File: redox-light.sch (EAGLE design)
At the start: 128 parts, among them IC36 STM32F103TXUX, X2 USBMICRO_B, X3 AUDIO-JACKSMD

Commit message: layout template
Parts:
- added IC38: 74HC595BQ, netcat:74HC595BQ
- added IC39: W25Q64FV, netcat:W25Q64FV
- C2: device netcat:CAP0402 -> netcat:CPOL-EUSMCA
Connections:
- removed net N$35: C1.+, IC37.IN, X2.VBUS
- new net FLASH_CS: IC36GPIOA.PA15, IC39.!CS
- new net SPI_MISO: IC36GPIOB.PB4, IC39.MISO/IO1
- new net SPI_MOSI: IC36GPIOB.PB5, IC39.MOSI/IO0
- new net SPI_SCL: IC36GPIOB.PB3, IC39.SCK
- new net SR_CLK: IC36GPIOB.PB1, IC38.SHCP, IC38.STCP
- new net SR_CLR: IC36GPIOB.PB2, IC38.!MR
- new net SR_D: IC36GPIOB.PB0, IC38.DS
- net !BL_EN: now also IC36GPIOA.PA8; no longer IC36GPIOB.PB5
- net 5V: now also C1.+, IC37.IN, X2.VBUS
- net BL_SDI: now also IC36GPIOA.PA7; no longer IC36GPIOA.PA8
- net GND: now also C2.-, IC38.!OE, IC38.GND, IC39.GND; no longer C2.2
- net N$17: now also VD4.C; no longer VD4.A
- net N$18: now also VD3.C; no longer VD3.A
- net N$19: now also VD5.C; no longer VD5.A
- net N$20: now also VD6.C; no longer VD6.A
- net N$21: now also VD2.C; no longer VD2.A
- net N$22: now also VD13.C; no longer VD13.A
- net N$24: now also VD7.C; no longer VD7.A
- net N$25: now also VD8.C; no longer VD8.A
- net N$26: now also VD9.C; no longer VD9.A
- net N$27: now also VD10.C; no longer VD10.A
- net N$28: now also VD11.C; no longer VD11.A
- net N$29: now also VD12.C; no longer VD12.A
- net N$30: now also VD20.C; no longer VD20.A
- net N$46: now also VD14.C; no longer VD14.A
- net N$47: now also VD15.C; no longer VD15.A
- net N$48: now also VD16.C; no longer VD16.A
- net N$49: now also VD17.C; no longer VD17.A
- net N$50: now also VD18.C; no longer VD18.A
- net N$51: now also VD19.C; no longer VD19.A
- net N$54: now also VD21.C; no longer VD21.A
- net N$55: now also VD22.C; no longer VD22.A
- net N$56: now also VD29.C; no longer VD29.A
- net N$57: now also VD30.C; no longer VD30.A
- net N$58: now also VD23.C; no longer VD23.A
- net N$59: now also VD24.C; no longer VD24.A
- net N$60: now also VD25.C; no longer VD25.A
- net N$61: now also VD26.C; no longer VD26.A
- net N$62: now also VD27.C; no longer VD27.A
- net N$63: now also VD28.C; no longer VD28.A
- net N$64: now also VD31.C; no longer VD31.A
- net N$65: now also VD32.C; no longer VD32.A
- net N$66: now also VD33.C; no longer VD33.A
- net N$67: now also VD34.C; no longer VD34.A
- net N$68: now also VD35.C; no longer VD35.A
- net N$7: now also VD1.C; no longer VD1.A
- net ROW0: now also IC38.Q0, VD1.A, VD13.A, VD2.A, VD3.A, VD4.A, VD5.A, VD6.A; no longer IC36GPIOB.PB0, VD1.C, VD13.C, VD2.C, VD3.C, VD4.C, VD5.C, VD6.C
- net ROW1: now also IC38.Q1, VD10.A, VD11.A, VD12.A, VD20.A, VD7.A, VD8.A, VD9.A; no longer IC36GPIOB.PB1, VD10.C, VD11.C, VD12.C, VD20.C, VD7.C, VD8.C, VD9.C
- net ROW2: now also IC38.Q2, VD14.A, VD15.A, VD16.A, VD17.A, VD18.A, VD19.A, VD27.A; no longer IC36GPIOB.PB2, VD14.C, VD15.C, VD16.C, VD17.C, VD18.C, VD19.C, VD27.C
- net ROW3: now also IC38.Q3, VD21.A, VD22.A, VD23.A, VD24.A, VD25.A, VD26.A, VD28.A; no longer IC36GPIOB.PB3, VD21.C, VD22.C, VD23.C, VD24.C, VD25.C, VD26.C, VD28.C
- net ROW4: now also IC38.Q4, VD29.A, VD30.A, VD31.A, VD32.A, VD33.A, VD34.A, VD35.A; no longer IC36GPIOB.PB4, VD29.C, VD30.C, VD31.C, VD32.C, VD33.C, VD34.C, VD35.C
- net VCC: now also C2.+, IC38.VCC, IC39.VCC; no longer C2.1
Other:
- moved on the sheet: VD1, VD10, VD11, VD12, VD13, VD14, VD15, VD16, VD17, VD18, VD19, VD2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

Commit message: aligned buttons, board layout completed
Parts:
- removed Q2: (no value), netcat:MOSFET_PSOT23
- removed R8: 100k, netcat:RESR0402
- removed X3: AUDIO-JACKSMD, netcat:AUDIO-JACKSMD
- removed X4: (no value), netcat:M03
- added C15, C16, C17, C18, C20, C21: (no value), netcat:CAP0402
- added C19: (no value), netcat:CPOL-EUSMCA
- added R2, R3: 4.7k, netcat:RESR0402
- added X1: USBMICRO_B, netcat:USBMICRO_B
- X2: value USBMICRO_B -> AUDIO-JACKSMD; device netcat:USBMICRO_B -> netcat:AUDIO-JACKSMD
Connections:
- removed net !BL_EN: IC36GPIOA.PA8, Q2.G, R8.2
- removed net VCC_LEDS: C10.1, C11.1, C12.1, C3.1, C4.1, C5.1, C6.1, C7.1, C8.1, C9.1, IC1.VCC, IC10.VCC, IC11.VCC, IC12.VCC, IC13.VCC, IC14.VCC, IC15.VCC, IC16.VCC, IC17.VCC, IC18.VCC, IC19.VCC, IC2.VCC, IC20.VCC, IC21.VCC, IC22.VCC, IC23.VCC, IC24.VCC, IC25.VCC, IC26.VCC, IC27.VCC, IC28.VCC, IC29.VCC, IC3.VCC, IC30.VCC, IC31.VCC, IC32.VCC, IC33.VCC, IC34.VCC, IC35.VCC, IC4.VCC, IC5.VCC, IC6.VCC, IC7.VCC, IC8.VCC, IC9.VCC, Q2.D
- net 5V: now also C10.1, C11.1, C12.1, C13.1, C14.1, C15.1, C16.1, C17.1, C18.1, C3.1, C4.1, C5.1, C6.1, C7.1, C8.1, C9.1, IC1.VCC, IC10.VCC, IC11.VCC, IC12.VCC, IC13.VCC, IC14.VCC, IC15.VCC, IC16.VCC, IC17.VCC, IC18.VCC, IC19.VCC, IC2.VCC, IC20.VCC, IC21.VCC, IC22.VCC, IC23.VCC, IC24.VCC, IC25.VCC, IC26.VCC, IC27.VCC, IC28.VCC, IC29.VCC, IC3.VCC, IC30.VCC, IC31.VCC, IC32.VCC, IC33.VCC, IC34.VCC, IC35.VCC, IC4.VCC, IC5.VCC, IC6.VCC, IC7.VCC, IC8.VCC, IC9.VCC, X1.VBUS, X2.4; no longer Q2.S, R8.1, X2.VBUS
- net BL_SDI: now also IC36GPIOA.PA8; no longer IC36GPIOA.PA7
- net GND: now also C15.2, C16.2, C17.2, C18.2, C19.-, C20.2, C21.2, IC36GPIOA.PA7, X1.GND, X2.1; no longer X2.GND, X3.1, X4.1
- net I2C_SCL: now also R2.2, X2.2; no longer X3.2
- net I2C_SDA: now also R3.2, X2.3; no longer X3.3
- net N$23: now also C20.1; no longer C13.1
- net N$31: now also C21.1; no longer C14.1
- net SWD_CLK: no longer X4.2
- net SWD_IO: no longer X4.3
- net USB_DM: now also X1.D-; no longer X2.D-
- net USB_DP: now also X1.D+; no longer X2.D+
- net VCC: now also IC39.!HOLD!/IO3, IC39.!WP!/IO2, R2.1, R3.1; no longer X3.4
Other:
- moved on the sheet: C10, C11, C12, C13, C14, C3, C4, C5, C6, C7, C8, C9

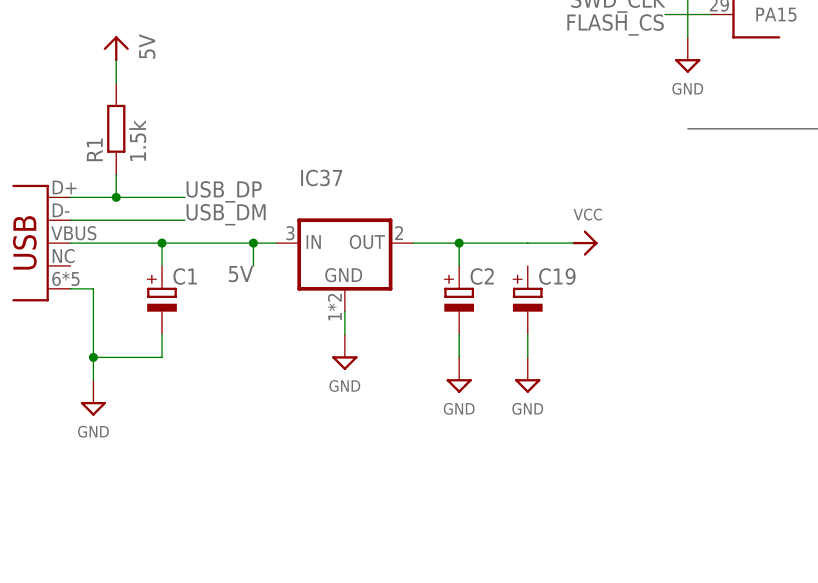
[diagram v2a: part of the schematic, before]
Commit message: layout, outline, silk update
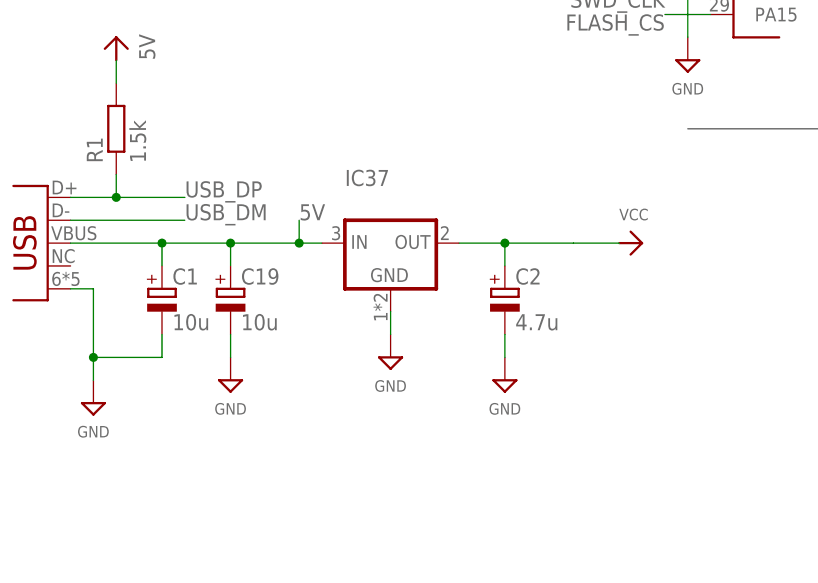
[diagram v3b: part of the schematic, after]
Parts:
- C1, C19: value (none) -> 10u
- C2: value (none) -> 4.7u
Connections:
- net 5V: now also C19.+
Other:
- moved on the sheet: C19, C2, IC37

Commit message: make schematic more simply, added SWD connector
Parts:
- removed IC38: 74HC595BQ, netcat:74HC595BQ
- removed IC39: W25Q64FV, netcat:W25Q64FV
- added X3: (no value), netcat:M03
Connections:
- removed net FLASH_CS: IC36GPIOA.PA15, IC39.!CS
- removed net SPI_MISO: IC36GPIOB.PB4, IC39.MISO/IO1
- removed net SPI_MOSI: IC36GPIOB.PB5, IC39.MOSI/IO0
- removed net SPI_SCL: IC36GPIOB.PB3, IC39.SCK
- removed net SR_CLK: IC36GPIOB.PB1, IC38.SHCP, IC38.STCP
- removed net SR_CLR: IC36GPIOB.PB2, IC38.!MR
- removed net SR_D: IC36GPIOB.PB0, IC38.DS
- net GND: now also X3.1; no longer IC38.!OE, IC38.GND, IC39.GND
- net ROW0: now also IC36GPIOB.PB0; no longer IC38.Q0
- net ROW1: now also IC36GPIOB.PB1; no longer IC38.Q1
- net ROW2: now also IC36GPIOB.PB2; no longer IC38.Q2
- net ROW3: now also IC36GPIOB.PB3; no longer IC38.Q3
- net ROW4: now also IC36GPIOB.PB4; no longer IC38.Q4
- net SWD_CLK: now also X3.2
- net SWD_IO: now also X3.3
- net VCC: no longer IC38.VCC, IC39.!HOLD!/IO3, IC39.!WP!/IO2, IC39.VCC
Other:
- moved on the sheet: C1, C10, C11, C12, C13, C14, C15, C16, C17, C18, C19, C2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

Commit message: silk layer update
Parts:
- removed C19: 10u, netcat:CPOL-EUSMCA
- added C22: 100n, netcat:CAP0402
- C10, C11, C12, C13, C14, C15, C16, C17, C18, C3, C4, C5, C6, C7, C8, C9: value (none) -> 100n
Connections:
- removed net UART_RX: IC36GPIOA.PA10
- removed net UART_TX: IC36GPIOA.PA9
- net 5V: no longer C19.+
- net GND: now also C22.2; no longer C19.-
- net VCC: now also C22.1
